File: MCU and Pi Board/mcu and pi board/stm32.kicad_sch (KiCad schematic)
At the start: 11 parts, among them J7 Conn_01x04_Pin, U1 STM32F091CCT6

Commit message: added some testpoints and some labeling
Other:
- note added: "Programming Header"
- moved on the sheet: J7
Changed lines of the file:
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@@
 	(generator_version "9.0")
 	(paper "A4")
+	(text "Programming Header"
+		(exclude_from_sim no)
+		(at 63.246 89.154 0)
+		(effects
+			(font
+				(size 1.27 1.27)
+			)
+		)
+	)
 	(junction
 		(at 210.82 81.28)
@@
 	(wire
 		(pts
-			(xy 77.47 83.82) (xy 73.66 83.82)
+			(xy 69.85 82.55) (xy 66.04 82.55)
 		)
 		(stroke
@@
 	(wire
 		(pts
-			(xy 77.47 81.28) (xy 73.66 81.28)
+			(xy 69.85 80.01) (xy 66.04 80.01)
 		)
 		(stroke
@@
 	)
 	(label "SWDIO "
-		(at 77.47 81.28 0)
+		(at 69.85 80.01 0)
 		(effects
 			(font
@@
 	)
 	(label "SWCLK "
-		(at 77.47 83.82 0)
+		(at 69.85 82.55 0)
 		(effects
 			(font
@@
 	(symbol
 		(lib_id "power:GND")
-		(at 73.66 78.74 90)
+		(at 66.04 77.47 90)
 		(unit 1)
 		(exclude_from_sim no)
@@
 		(fields_autoplaced yes)
 		(property "Reference" "#PWR028"
-			(at 80.01 78.74 0)
+			(at 72.39 77.47 0)
 			(effects
 				(font
@@
 		)
 		(property "Value" "GND"
-			(at 77.47 78.7399 90)
+			(at 69.85 77.4699 90)
 			(effects
 				(font
@@
 		)
 		(property "Footprint" ""
-			(at 73.66 78.74 0)
+			(at 66.04 77.47 0)
 			(effects
 				(font
@@
 		)
 		(property "Datasheet" ""
-			(at 73.66 78.74 0)
+			(at 66.04 77.47 0)
 			(effects
 				(font
@@
 		)
 		(property "Description" "Power symbol creates a global label with name \"GND\" , ground"
-			(at 73.66 78.74 0)
+			(at 66.04 77.47 0)
 			(effects
 				(font
@@
 	(symbol
 		(lib_id "power:+3.3V")
-		(at 73.66 86.36 270)
+		(at 66.04 85.09 270)
 		(unit 1)
 		(exclude_from_sim no)
@@
 		(fields_autoplaced yes)
 		(property "Reference" "#PWR029"
-			(at 69.85 86.36 0)
+			(at 62.23 85.09 0)
 			(effects
 				(font
@@
 		)
 		(property "Value" "+3.3V"
-			(at 77.47 86.3599 90)
+			(at 69.85 85.0899 90)
 			(effects
 				(font
@@
 		)
 		(property "Footprint" ""
-			(at 73.66 86.36 0)
+			(at 66.04 85.09 0)
 			(effects
 				(font
@@
 		)
 		(property "Datasheet" ""
-			(at 73.66 86.36 0)
+			(at 66.04 85.09 0)
 			(effects
 				(font
@@
 		)
 		(property "Description" "Power symbol creates a global label with name \"+3.3V\""
-			(at 73.66 86.36 0)
+			(at 66.04 85.09 0)
 			(effects
 				(font
@@
 	(symbol
 		(lib_id "Connector:Conn_01x04_Pin")
-		(at 68.58 81.28 0)
+		(at 60.96 80.01 0)
 		(unit 1)
 		(exclude_from_sim no)
@@
 		(fields_autoplaced yes)
 		(property "Reference" "J7"
-			(at 69.215 73.66 0)
+			(at 61.595 72.39 0)
 			(effects
 				(font
@@
 		)
 		(property "Value" "Conn_01x04_Pin"
-			(at 69.215 76.2 0)
+			(at 61.595 74.93 0)
 			(effects
 				(font
@@
 		)
 		(property "Footprint" ""
-			(at 68.58 81.28 0)
+			(at 60.96 80.01 0)
 			(effects
 				(font
@@
 		)
 		(property "Datasheet" "~"
-			(at 68.58 81.28 0)
+			(at 60.96 80.01 0)
 			(effects
 				(font
@@
 		)
 		(property "Description" "Generic connector, single row, 01x04, script generated"
-			(at 68.58 81.28 0)
-			(effects
-				(font
+			(at 60.96 80.01 0)
+			(effects
+				(font

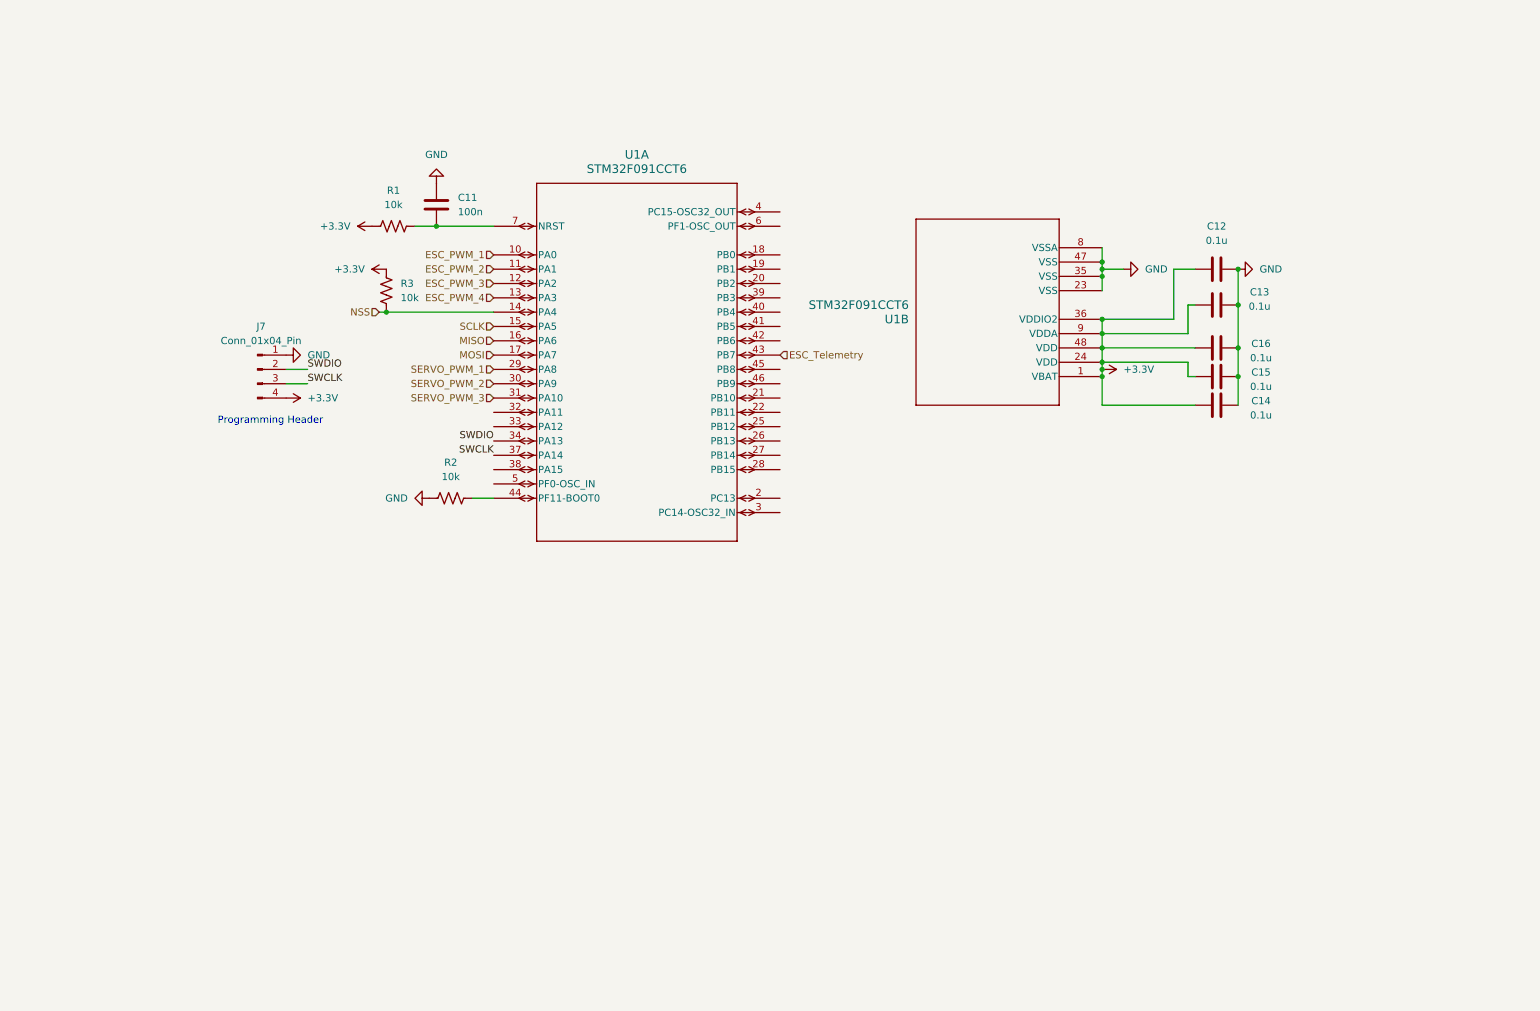
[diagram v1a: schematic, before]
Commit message: added leds and minor fixes
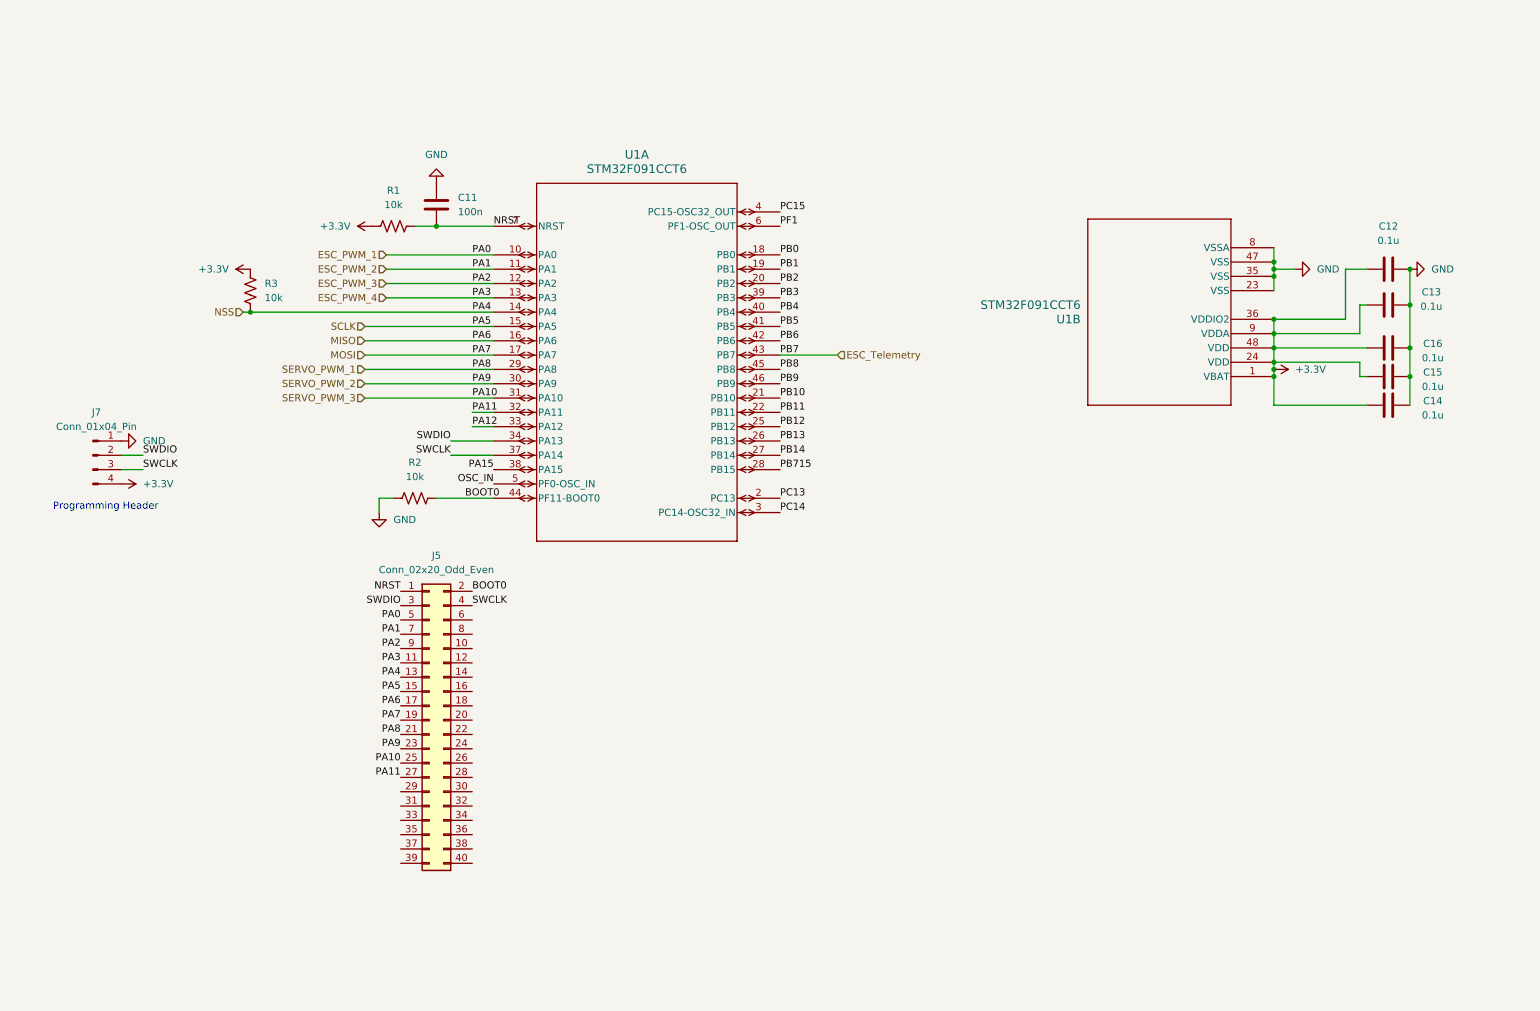
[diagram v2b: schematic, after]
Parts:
- added J5: Conn_02x20_Odd_Even, symbol Connector_Generic:Conn_02x20_Odd_Even
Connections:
- net ESC_PWM_1: now also J5.5 (Pin_5)
- net ESC_PWM_2: now also J5.7 (Pin_7)
- net ESC_PWM_3: now also J5.9 (Pin_9)
- net ESC_PWM_4: now also J5.11 (Pin_11)
- net MISO: now also J5.17 (Pin_17)
- net MOSI: now also J5.19 (Pin_19)
- net NSS: now also J5.13 (Pin_13)
- net SCLK: now also J5.15 (Pin_15)
- net SERVO_PWM_1: now also J5.21 (Pin_21)
- net SERVO_PWM_2: now also J5.23 (Pin_23)
- net SERVO_PWM_3: now also J5.25 (Pin_25)
- net SWCLK : now also J5.4 (Pin_4)
- net SWDIO : now also J5.3 (Pin_3)
- net NRST: now reaches C11.2, R1.2, U1.7 (NRST)
- net NRST: now also J5.1 (Pin_1)
- net PB0: now reaches U1.18 (PB0)
- net PB1: now reaches U1.19 (PB1)
- net PC13: now reaches U1.2 (PC13)
- net PB2: now reaches U1.20 (PB2)
- net PB10: now reaches U1.21 (PB10)
- net PB11: now reaches U1.22 (PB11)
- net PB12: now reaches U1.25 (PB12)
- net PB13: now reaches U1.26 (PB13)
- net PB14: now reaches U1.27 (PB14)
- net PB715: now reaches U1.28 (PB15)
- net PC14: now reaches U1.3 (PC14-OSC32_IN)
- net PA11: now reaches U1.32 (PA11)
- net PA11: now also J5.27 (Pin_27)
- net PA12: now reaches U1.33 (PA12)
- net PA15: now reaches U1.38 (PA15)
- net PB3: now reaches U1.39 (PB3)
- net PC15: now reaches U1.4 (PC15-OSC32_OUT)
- net PB4: now reaches U1.40 (PB4)
- net PB5: now reaches U1.41 (PB5)
- net PB6: now reaches U1.42 (PB6)
- net BOOT0: now reaches R2.2, U1.44 (PF11-BOOT0)
- net BOOT0: now also J5.2 (Pin_2)
- net PB8: now reaches U1.45 (PB8)
- net PB9: now reaches U1.46 (PB9)
- net OSC_IN: now reaches U1.5 (PF0-OSC_IN)
- net PF1: now reaches U1.6 (PF1-OSC_OUT)
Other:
- moved on the sheet: C12, C13, C14, C15, C16, J7, R2, R3, U1B

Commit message: pretty much done i think
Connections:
- net PB715 is gone; now on net PB15: U1.28 (PB15)
- net ESC_Telemetry: now also J5.20 (Pin_20)
- net OSC_IN: now also J5.37 (Pin_37)
- net PA12: now also J5.29 (Pin_29)
- net PA15: now also J5.31 (Pin_31)
- net PB0: now also J5.6 (Pin_6)
- net PB1: now also J5.8 (Pin_8)
- net PB10: now also J5.26 (Pin_26)
- net PB11: now also J5.28 (Pin_28)
- net PB12: now also J5.30 (Pin_30)
- net PB13: now also J5.32 (Pin_32)
- net PB14: now also J5.34 (Pin_34)
- net PB2: now also J5.10 (Pin_10)
- net PB3: now also J5.12 (Pin_12)
- net PB4: now also J5.14 (Pin_14)
- net PB5: now also J5.16 (Pin_16)
- net PB6: now also J5.18 (Pin_18)
- net PB8: now also J5.22 (Pin_22)
- net PB9: now also J5.24 (Pin_24)
- net PC13: now also J5.38 (Pin_38)
- net PC14: now also J5.40 (Pin_40)
- net PC15: now also J5.35 (Pin_35)
- net PF1: now also J5.33 (Pin_33)
- net PB15: now reaches J5.36 (Pin_36)
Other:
- moved on the sheet: C12, C13, C14, C15, C16, J5, J7, U1B

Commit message: pretty much done
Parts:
- added J15, J16, J19, J20: Conn_01x28_Socket, symbol Connector:Conn_01x28_Socket
- added J17: DebugnBoot, Connector_PinHeader_2.54mm:PinHeader_1x04_P2.54mm_Vertical, symbol Connector:Conn_01x04_Pin
- added J18: UART-PINS, Connector_PinHeader_2.54mm:PinHeader_1x03_P2.54mm_Vertical, symbol Connector:Conn_01x03_Pin
- added R18, R19: 10k, symbol Device:R_US
- added SW1: SW_Push, symbol Switch:SW_Push
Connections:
- net +3.3V: now also R18.2
- net GND: now also J15.28 (Pin_28), J16.1 (Pin_1), J19.1 (Pin_1), J20.28 (Pin_28), R19.2
- net MISO: now also J16.14 (Pin_14), J19.14 (Pin_14)
- net MOSI: now also J16.15 (Pin_15), J19.15 (Pin_15)
- net NRST: now also SW1.1
- net SCLK: now also J16.16 (Pin_16), J19.16 (Pin_16)
- net ESC_PWM_1 renamed STM_ESC_PWM_0
- net ESC_PWM_2 renamed STM_ESC_PWM_1
- net ESC_PWM_3 renamed STM_ESC_PWM_2
- net ESC_PWM_4 renamed STM_ESC_PWM_3
- net NSS renamed STM_CS
- net PB6 renamed SCL
- net SCL: now also J16.11 (Pin_11), J19.11 (Pin_11)
- net PB9 renamed SDA
- net SDA: now also J16.12 (Pin_12), J19.12 (Pin_12)
- net SERVO_PWM_1 renamed STM_SERVO_PWM_0
- net SERVO_PWM_2 renamed STM_SERVO_PWM_1
- net SERVO_PWM_3 renamed STM_SERVO_PWM_2
- new net: R19.1, SW1.2
- new net GPIO0: J16.26 (Pin_26), J18.3 (Pin_3), J19.26 (Pin_26)
- new net GPIO1: J16.25 (Pin_25), J18.1 (Pin_1), J19.25 (Pin_25)
- new net GPIO13: J16.13 (Pin_13), J19.13 (Pin_13)
- new net GPIO16: J16.10 (Pin_10), J19.10 (Pin_10)
- new net GPIO17: J16.9 (Pin_9), J19.9 (Pin_9)
- new net GPIO18: J16.8 (Pin_8), J19.8 (Pin_8)
- new net GPIO19: J16.7 (Pin_7), J19.7 (Pin_7)
- new net GPIO20: J16.6 (Pin_6), J19.6 (Pin_6)
- new net GPIO21: J16.5 (Pin_5), J19.5 (Pin_5)
- new net GPIO22: J16.4 (Pin_4), J19.4 (Pin_4)
- new net GPIO23: J16.3 (Pin_3), J19.3 (Pin_3)
- new net GPIO24: J16.2 (Pin_2), J19.2 (Pin_2)
- new net GPIO25: J15.25 (Pin_25), J20.25 (Pin_25)
- new net GPIO26: J15.24 (Pin_24), J20.24 (Pin_24)
- new net GPIO27: J15.23 (Pin_23), J20.23 (Pin_23)
- new net GPIO28: J15.22 (Pin_22), J20.22 (Pin_22)
- new net GPIO29: J15.21 (Pin_21), J20.21 (Pin_21)
- new net GPIO30: J15.20 (Pin_20), J20.20 (Pin_20)
- new net GPIO31: J15.19 (Pin_19), J20.19 (Pin_19)
- new net GPIO32: J15.18 (Pin_18), J20.18 (Pin_18)
- new net GPIO33: J15.17 (Pin_17), J20.17 (Pin_17)
- new net GPIO34: J15.16 (Pin_16), J20.16 (Pin_16)
- new net GPIO35: J15.15 (Pin_15), J20.15 (Pin_15)
- new net GPIO36: J15.14 (Pin_14), J20.14 (Pin_14)
- new net GPIO37: J15.13 (Pin_13), J20.13 (Pin_13)
- new net GPIO38: J15.12 (Pin_12), J20.12 (Pin_12)
- new net GPIO39: J15.11 (Pin_11), J20.11 (Pin_11)
- new net GPIO40_ADC0: J15.10 (Pin_10), J20.10 (Pin_10)
- new net GPIO41_ADC1: J15.9 (Pin_9), J20.9 (Pin_9)
- new net GPIO42_ADC2: J15.8 (Pin_8), J20.8 (Pin_8)
- new net GPIO43_ADC3: J15.7 (Pin_7), J20.7 (Pin_7)
- new net GPIO44_ADC4: J15.6 (Pin_6), J20.6 (Pin_6)
- new net GPIO45_ADC5: J15.5 (Pin_5), J20.5 (Pin_5)
- new net GPIO46_ADC6: J15.4 (Pin_4), J20.4 (Pin_4)
- new net GPIO47_ADC7: J15.3 (Pin_3), J20.3 (Pin_3)
- new net PGND: J17.3 (Pin_3), J18.2 (Pin_2)
- new net RP2350B_CS: J16.17 (Pin_17), J19.17 (Pin_17), R18.1
- new net RP2350B_ESC_PWM_0: J16.24 (Pin_24), J19.24 (Pin_24)
- new net RP2350B_ESC_PWM_1: J16.23 (Pin_23), J19.23 (Pin_23)
- new net RP2350B_ESC_PWM_2: J16.22 (Pin_22), J19.22 (Pin_22)
- new net RP2350B_ESC_PWM_3: J16.21 (Pin_21), J19.21 (Pin_21)
- new net RP2350B_SERVO_PWM_0: J16.20 (Pin_20), J19.20 (Pin_20)
- new net RP2350B_SERVO_PWM_1: J16.19 (Pin_19), J19.19 (Pin_19)
- new net RP2350B_SERVO_PWM_2: J16.18 (Pin_18), J19.18 (Pin_18)
- new net SWCLK: J15.26 (Pin_26), J20.26 (Pin_26)
- new net SWD: J15.27 (Pin_27), J20.27 (Pin_27)
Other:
- moved on the sheet: R1

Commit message: started routing
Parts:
- removed J19, J20: Conn_01x28_Socket, symbol Connector:Conn_01x28_Socket
- removed SW1: SW_Push, symbol Switch:SW_Push
- added S1: TS04-66-70-BK-160-SMT, custom library:SW_TS04-66-70-BK-160-SMT, symbol custom library:TS04-66-70-BK-160-SMT
- C11: value 100n -> 0.1u; footprint (none) -> Capacitor_SMD:C_0603_1608Metric_Pad1.08x0.95mm_HandSolder
- C12, C13, C14, C15, C16: footprint (none) -> Capacitor_SMD:C_0603_1608Metric_Pad1.08x0.95mm_HandSolder
- J15, J16: footprint (none) -> Connector_PinSocket_2.54mm:PinSocket_1x28_P2.54mm_Vertical
- J5: footprint (none) -> Connector_PinHeader_2.54mm:PinHeader_2x20_P2.54mm_Vertical
- J7: footprint (none) -> Connector_PinHeader_2.54mm:PinHeader_1x04_P2.54mm_Vertical
- R1, R18, R19, R2, R3: footprint (none) -> Resistor_SMD:R_0603_1608Metric_Pad0.98x0.95mm_HandSolder
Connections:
- net GPIO13 is gone; now on net ESC_Telemetry: J16.13 (Pin_13)
- net PGND is gone; now on net GND: J17.3 (Pin_3), J18.2 (Pin_2)
- net NRST: now also S1.2
- net at R19.1: now also S1.1
- no-connect marks 0 -> 5
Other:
- moved on the sheet: R19

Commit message: yeet
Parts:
- removed J5: Conn_02x20_Odd_Even, Connector_PinHeader_2.54mm:PinHeader_2x20_P2.54mm_Vertical, symbol Connector_Generic:Conn_02x20_Odd_Even
- added J19, J32, J33: Conn_01x02_Pin, Connector_PinHeader_2.54mm:PinHeader_1x02_P2.54mm_Vertical, symbol Connector:Conn_01x02_Pin
- added J20, J34: Conn_01x03_Pin, Connector_PinHeader_2.54mm:PinHeader_1x03_P2.54mm_Vertical, symbol Connector:Conn_01x03_Pin
- added J21: Conn_01x05, Connector_PinSocket_2.54mm:PinSocket_1x05_P2.54mm_Vertical, symbol Connector_Generic:Conn_01x05
- added J26: Conn_01x03_Pin, Connector_PinSocket_2.54mm:PinSocket_1x03_P2.54mm_Vertical, symbol Connector:Conn_01x03_Pin
- added J27: Conn_01x02_Pin, Connector_PinSocket_2.54mm:PinSocket_1x02_P2.54mm_Vertical, symbol Connector:Conn_01x02_Pin
- added J30, J31: Conn_01x04_Pin, Connector_PinHeader_2.54mm:PinHeader_1x04_P2.54mm_Vertical, symbol Connector:Conn_01x04_Pin
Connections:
- net PB1 is gone; now on net STM_SERVO_PWM_0: U1.19 (PB1)
- net PB3 is gone; now on net STM_SERVO_PWM_1: U1.39 (PB3)
- net PB4 is gone; now on net STM_SERVO_PWM_2: U1.40 (PB4)
- net PB5 is gone; now on net STM_ESC_PWM_3: U1.41 (PB5)
- net ESC_Telemetry: now also U1.10 (PA0), J21.5 (Pin_5); no longer U1.43 (PB7)
- net MISO: now also J31.3 (Pin_3)
- net MOSI: now also J31.4 (Pin_4)
- net PA11: now also J20.1 (Pin_1)
- net PA12: now also J20.2 (Pin_2)
- net PA15: now also J20.3 (Pin_3)
- net PB0: now also J34.2 (Pin_2)
- net PB2: now also J34.3 (Pin_3)
- net PB8: now also J33.1 (Pin_1)
- net SCL: now also J32.1 (Pin_1)
- net SCLK: now also J31.2 (Pin_2)
- net SDA: now also U1.43 (PB7), J32.2 (Pin_2); no longer U1.46 (PB9)
- net STM_CS: now also J31.1 (Pin_1)
- net STM_ESC_PWM_0: now also U1.12 (PA2), J21.1 (Pin_1); no longer U1.10 (PA0)
- net STM_ESC_PWM_1: now also U1.13 (PA3), J21.2 (Pin_2); no longer U1.11 (PA1)
- net STM_ESC_PWM_2: now also U1.29 (PA8), J21.3 (Pin_3); no longer U1.12 (PA2)
- net STM_ESC_PWM_3: now also J21.4 (Pin_4); no longer U1.13 (PA3)
- net STM_SERVO_PWM_0: now also J26.1 (Pin_1); no longer U1.29 (PA8)
- net STM_SERVO_PWM_1: now also J26.2 (Pin_2); no longer U1.30 (PA9)
- net STM_SERVO_PWM_2: now also J26.3 (Pin_3); no longer U1.31 (PA10)
- net OSC_IN: no longer names the net of U1.5 (PF0-OSC_IN)
- net PB10 renamed SCL_BREAKOUT
- net SCL_BREAKOUT: now also J19.2 (Pin_2)
- net PB11 renamed SDA_BREAKOUT
- net SDA_BREAKOUT: now also J19.1 (Pin_1)
- net PB12 renamed CS_BREAKOUT
- net CS_BREAKOUT: now also J30.1 (Pin_1)
- net PB13 renamed SCK_BREAKOUT
- net SCK_BREAKOUT: now also J30.2 (Pin_2)
- net PB14 renamed MISO_BREAKOUT
- net MISO_BREAKOUT: now also J30.3 (Pin_3)
- net PB15 renamed MOSI_BREAKOUT
- net MOSI_BREAKOUT: now also J30.4 (Pin_4)
- net PC13: no longer names the net of U1.2 (PC13)
- net PC14: no longer names the net of U1.3 (PC14-OSC32_IN)
- net PC15: no longer names the net of U1.4 (PC15-OSC32_OUT)
- net PF1: no longer names the net of U1.6 (PF1-OSC_OUT)
- new net PA1: J34.1 (Pin_1), U1.11 (PA1)
- new net PA10: J27.1 (Pin_1), U1.31 (PA10)
- new net PA9: J27.2 (Pin_2), U1.30 (PA9)
- new net PB9: J33.2 (Pin_2), U1.46 (PB9)
- no-connect marks 5 -> 9
